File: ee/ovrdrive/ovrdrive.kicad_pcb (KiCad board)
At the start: 2 copper layers, 47.2 x 15.1 mm, 6 parts, among them J1 USB_A, U1 SM3257ENT, U2 JDEC_FLASH

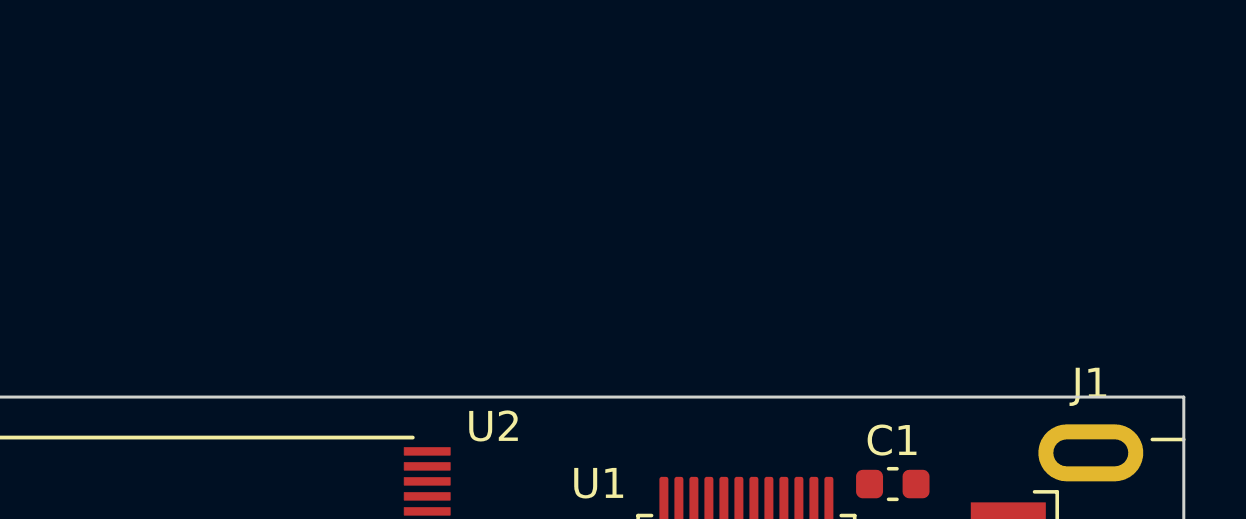
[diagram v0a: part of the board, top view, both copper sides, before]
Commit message: Updated the sm3257en to the correct pinout. Dropped some parts on the layout.
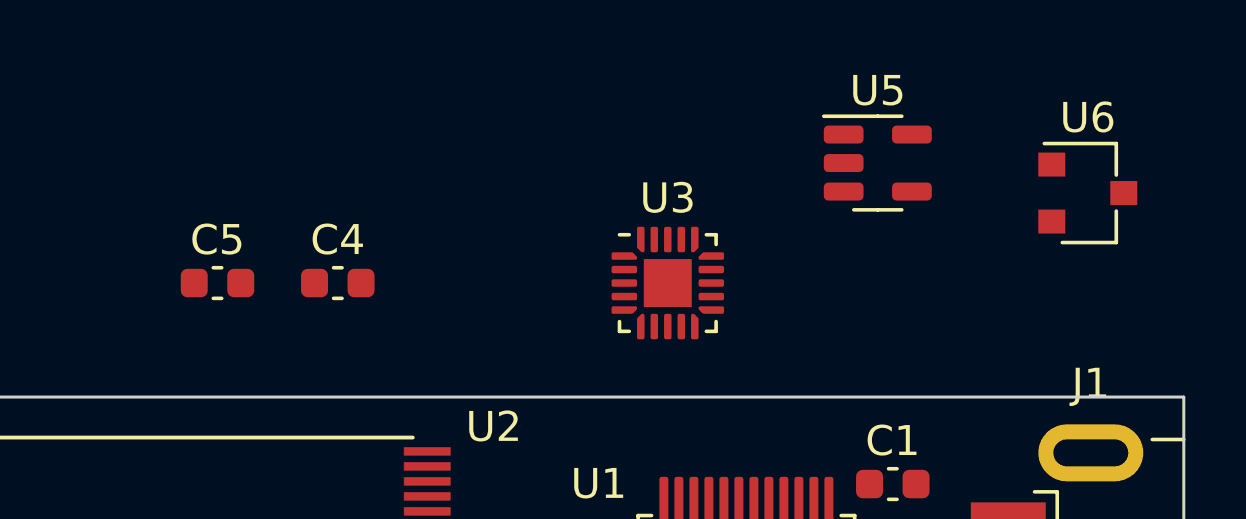
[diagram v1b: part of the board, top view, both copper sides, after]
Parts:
- added C4: 100nF, Capacitor_SMD:C_0603_1608Metric, F.Cu at (121.0, 75.0)
- added C5: 4.7uF, Capacitor_SMD:C_0603_1608Metric, F.Cu at (117.0, 75.0)
- added U3: ATtiny24A-MM, Package_DFN_QFN:QFN-20-1EP_3x3mm_P0.45mm_EP1.6x1.6mm, F.Cu at (132.0, 75.0)
- added U5: AD8001AR, Package_TO_SOT_SMD:SOT-23-5, F.Cu at (139.0, 71.0)
- added U6: TL431DCK, Package_TO_SOT_SMD:SC-59, F.Cu at (146.0, 72.0)
- U2: value JDEC_FLASH -> FLASH
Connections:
- C3 pad 1: unconnected-(C3-Pad1) -> +3.3V
- C3 pad 2: unconnected-(C3-Pad2) -> GND
- J1 pad 1: unconnected-(J1-Pad1) -> +5V
- J1 pad 4: unconnected-(J1-Pad4) -> GND
- J1 pad 5: unconnected-(J1-Pad5) -> GND
- U1 pad 22: unconnected-(U1-Pad22) -> GND
- U1 pad 36: unconnected-(U1-Pad36) -> GND
- U1 pad 37: unconnected-(U1-Pad37) -> +5V
- U1 pad 41: unconnected-(U1-Pad41) -> GND
- U1 pad 46: unconnected-(U1-Pad46) -> GND
- U1 pad 47: unconnected-(U1-Pad47) -> GND
- U1 pad 9: unconnected-(U1-Pad9) -> GND
- U2 pad 12: unconnected-(U2-Pad12) -> +3.3V
- U2 pad 13: unconnected-(U2-Pad13) -> GND
- U2 pad 36: unconnected-(U2-Pad36) -> GND
- U2 pad 37: unconnected-(U2-Pad37) -> +3.3V
- U2 pad 9: /~{CE} -> Net-(U2-Pad9)

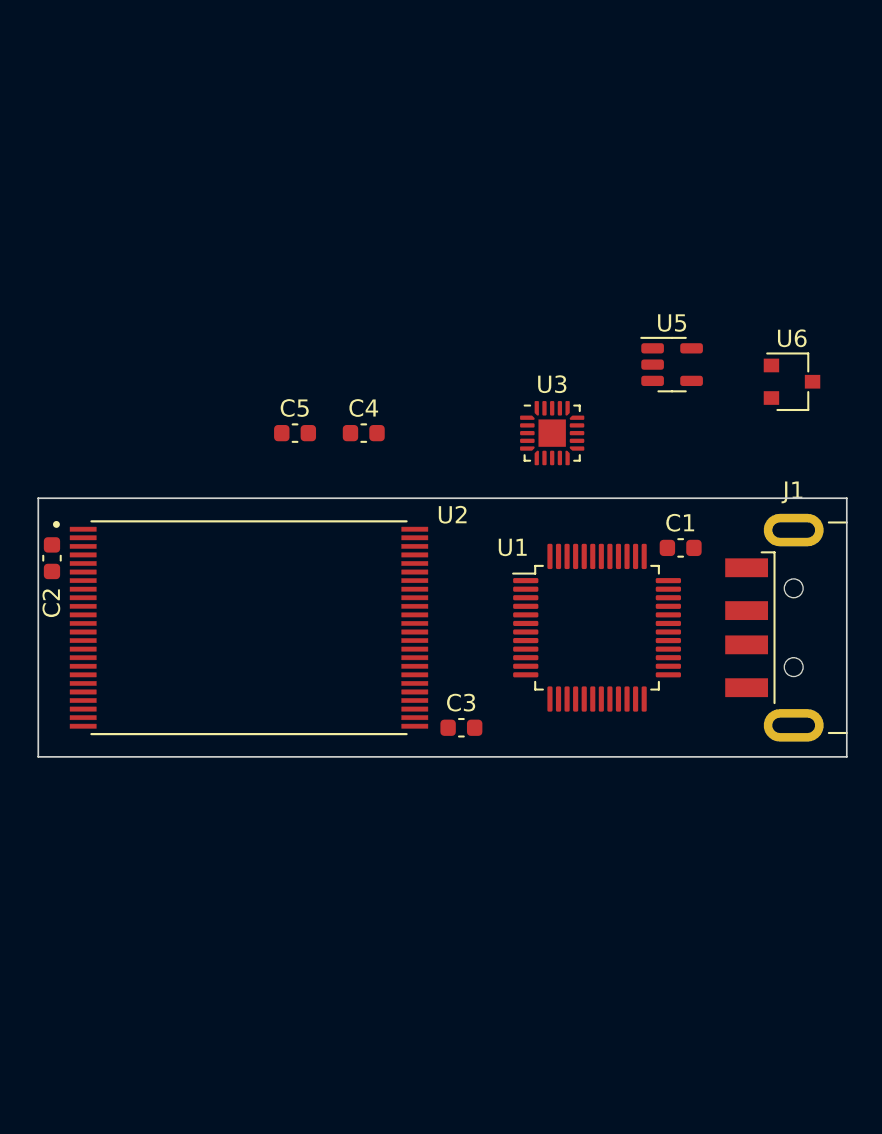
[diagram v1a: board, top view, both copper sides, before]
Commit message: Added a bunch of mech parts.
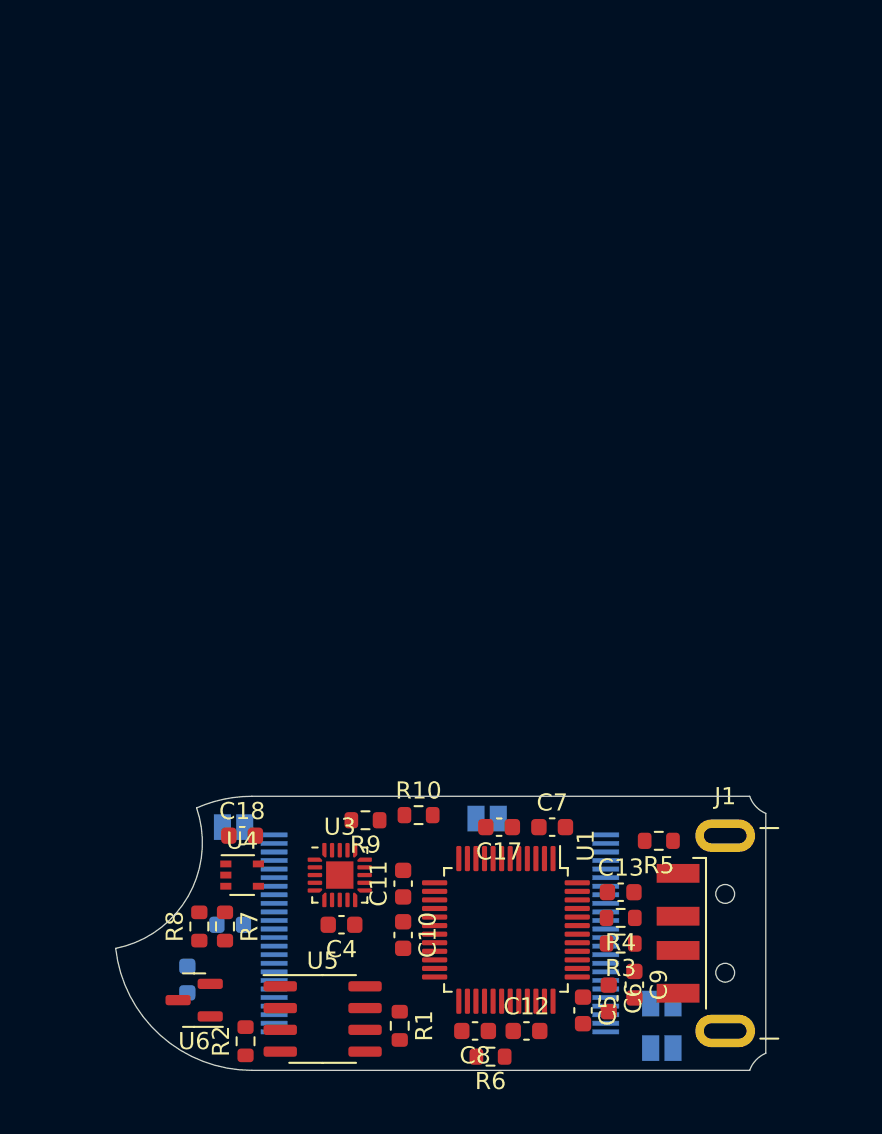
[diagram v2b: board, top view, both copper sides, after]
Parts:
- removed C3: 1uF, Capacitor_SMD:C_0603_1608Metric
- added C10: 1uF, Capacitor_SMD:C_0603_1608Metric, F.Cu at (123.3, 104.3)
- added C11: 1uF, Capacitor_SMD:C_0603_1608Metric, F.Cu at (123.3, 101.3)
- added C12: 1uF, Capacitor_SMD:C_0603_1608Metric, F.Cu at (130.5, 109.9)
- added C13: 1uF, Capacitor_SMD:C_0603_1608Metric, F.Cu at (136.0, 101.8)
- added C17: 1uF, Capacitor_SMD:C_0603_1608Metric, F.Cu at (128.9, 98.0)
- added C18: 100nF, Capacitor_SMD:C_0603_1608Metric, F.Cu at (113.9, 98.5)
- added C6: 4.7uF, Capacitor_SMD:C_0603_1608Metric, F.Cu at (135.3, 108.0)
- added C7: 4.7uF, Capacitor_SMD:C_0603_1608Metric, F.Cu at (132.0, 98.0)
- added C8: 1uF, Capacitor_SMD:C_0603_1608Metric, F.Cu at (127.5, 109.9)
- added C9: 1uF, Capacitor_SMD:C_0603_1608Metric, F.Cu at (136.8, 107.2)
- added JP1: SolderJumper_2_Open, Jumper:SolderJumper-2_P1.3mm_Open_Pad1.0x1.5mm, B.Cu at (138.4, 108.3)
- added JP2: SolderJumper_2_Open, Jumper:SolderJumper-2_P1.3mm_Open_Pad1.0x1.5mm, B.Cu at (138.4, 110.9)
- added JP3: SolderJumper_2_Open, Jumper:SolderJumper-2_P1.3mm_Open_Pad1.0x1.5mm, B.Cu at (113.4, 98.0)
- added JP4: SolderJumper_2_Open, Jumper:SolderJumper-2_P1.3mm_Open_Pad1.0x1.5mm, B.Cu at (128.2, 97.5)
- added R1: 10k, Resistor_SMD:R_0603_1608Metric, F.Cu at (123.1, 109.6)
- added R10: 680R, Resistor_SMD:R_0603_1608Metric, F.Cu at (124.2, 97.3)
- added R2: 747k, Resistor_SMD:R_0603_1608Metric, F.Cu at (114.1, 110.5)
- added R3: 2.2R, Resistor_SMD:R_0603_1608Metric, F.Cu at (136.0, 104.8)
- added R4: 2.2R, Resistor_SMD:R_0603_1608Metric, F.Cu at (136.0, 103.3)
- added R5: 2.2R, Resistor_SMD:R_0603_1608Metric, F.Cu at (138.2, 98.8)
- added R6: 1k, Resistor_SMD:R_0603_1608Metric, F.Cu at (128.4, 111.4)
- added R7: 10k, Resistor_SMD:R_0603_1608Metric, F.Cu at (112.9, 103.8)
- added R8: 10k, Resistor_SMD:R_0603_1608Metric, F.Cu at (111.4, 103.8)
- added R9: 1k, Resistor_SMD:R_0603_1608Metric, F.Cu at (121.1, 97.6)
- added U4: 74AUC1G32, Package_TO_SOT_SMD:SOT-353_SC-70-5, F.Cu at (113.9, 100.8)
- C1: value 1uF -> 100nF; moved to B.Cu
- C2, U2: moved to B.Cu
- C4: value 100nF -> 1uF
- U5: footprint Package_TO_SOT_SMD:SOT-23-5 -> Package_SO:SOIC-8_3.9x4.9mm_P1.27mm
- U6: value TL431DCK -> LM4040DBZ-2.5; footprint Package_TO_SOT_SMD:SC-59 -> Package_TO_SOT_SMD:SOT-23
- moved U6 50.2 mm to (111.1, 108.1), turned to 180 degrees
- moved U5 43.3 mm to (118.6, 109.2)
- moved C5 37.7 mm to (133.8, 108.7), turned to -90 degrees
- moved C1 34.3 mm to (113.2, 103.7), turned to 180 degrees
- moved C4 28.7 mm to (119.7, 103.7), turned to 180 degrees
- moved U3 28.6 mm to (119.6, 100.8)
- moved C2 25.8 mm to (110.7, 106.9)
- moved U2 21.0 mm to (125.4, 104.2), turned to 180 degrees
- moved U1 18.4 mm to (129.3, 104.0), turned to -90 degrees
- moved J1 18.3 mm to (149.0, 104.2)
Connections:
- C1 pad 1: unconnected-(C1-Pad1) -> +3.3V
- C1 pad 2: unconnected-(C1-Pad2) -> GND
- C2 pad 1: unconnected-(C2-Pad1) -> +3.3V
- C2 pad 2: unconnected-(C2-Pad2) -> GND
- C4 pad 1: +3.3V -> +5V
- J1 pad 1: +5V -> Net-(J1-Pad1)
- J1 pad 2: unconnected-(J1-Pad2) -> Net-(J1-Pad2)
- J1 pad 3: unconnected-(J1-Pad3) -> Net-(J1-Pad3)
- U1 pad 14: unconnected-(U1-Pad14) -> +3.3V
- U1 pad 15: unconnected-(U1-Pad15) -> +3.3V
- U1 pad 16: unconnected-(U1-Pad16) -> +1V8
- U1 pad 17: unconnected-(U1-Pad17) -> +3.3V
- U1 pad 2: unconnected-(U1-Pad2) -> /RB1
- U1 pad 27: unconnected-(U1-Pad27) -> Net-(R6-Pad2)
- U1 pad 28: unconnected-(U1-Pad28) -> +3.3V
- U1 pad 29: unconnected-(U1-Pad29) -> +1V8
- U1 pad 3: unconnected-(U1-Pad3) -> +1V8
- U1 pad 30: unconnected-(U1-Pad30) -> +3.3V
- U1 pad 31: unconnected-(U1-Pad31) -> /DQS
- U1 pad 32: unconnected-(U1-Pad32) -> Net-(JP1-Pad2)
- U1 pad 33: unconnected-(U1-Pad33) -> Net-(JP2-Pad2)
- U1 pad 34: unconnected-(U1-Pad34) -> /~{CE3}
- U1 pad 35: unconnected-(U1-Pad35) -> /~{CE2}
- U1 pad 38: unconnected-(U1-Pad38) -> +3.3V
- U1 pad 39: unconnected-(U1-Pad39) -> +3.3V
- U1 pad 4: unconnected-(U1-Pad4) -> +3.3V
- U1 pad 40: unconnected-(U1-Pad40) -> +1V8
- U1 pad 42: unconnected-(U1-Pad42) -> /DM
- U1 pad 43: unconnected-(U1-Pad43) -> /DP
- U1 pad 44: unconnected-(U1-Pad44) -> Net-(JP4-Pad2)
- U1 pad 45: unconnected-(U1-Pad45) -> +3.3V
- U1 pad 5: unconnected-(U1-Pad5) -> /RB0
- U1 pad 8: unconnected-(U1-Pad8) -> /~{CE1}
- U3 pad 1: unconnected-(U3-Pad1) -> /SCK
- U3 pad 13: unconnected-(U3-Pad13) -> /~{RST}
- U3 pad 15: unconnected-(U3-Pad15) -> Net-(D1-Pad2)
- U3 pad 16: unconnected-(U3-Pad16) -> /MOSI
- U3 pad 20: unconnected-(U3-Pad20) -> /MISO
- U3 pad 21: Net-(U3-Pad21) -> GND
- U3 pad 3: unconnected-(U3-Pad3) -> Net-(R7-Pad2)
- U3 pad 4: unconnected-(U3-Pad4) -> /Vs
- U3 pad 8: Net-(U3-Pad21) -> GND
- U3 pad 9: unconnected-(U3-Pad9) -> +5V
- U5 pad 2: unconnected-(U5-Pad2) -> /Vs
- U5 pad 3: unconnected-(U5-Pad3) -> Net-(J2-Pad2)
- U5 pad 4: unconnected-(U5-Pad4) -> GND
- U6 pad 1: unconnected-(U6-Pad1) -> Net-(R1-Pad2)
- U6 pad 2: (no net) -> /Vs
- U6 pad 3: unconnected-(U6-Pad3) -> (no net)
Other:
- board size 47.2 x 15.1 mm -> 38 x 16 mm

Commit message: Mech looking decent, new USB to fit in case.
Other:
- copper layers 2 -> 4
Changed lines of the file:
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@@
 (kicad_pcb (version 20211014) (generator pcbnew)
   (general
-    (thickness 1.6)
+    (thickness 0.799)
   )
   (paper "A4")
   (layers
     (0 "F.Cu" signal)
+    (1 "In1.Cu" signal)
+    (2 "In2.Cu" signal)
     (31 "B.Cu" signal)
     (32 "B.Adhes" user "B.Adhesive")
@@
   )
   (setup
+    (stackup
+      (layer "F.SilkS" (type "Top Silk Screen"))
+      (layer "F.Paste" (type "Top Solder Paste"))
+      (layer "F.Mask" (type "Top Solder Mask") (thickness 0.01))
+      (layer "F.Cu" (type "copper") (thickness 0.035))
+      (layer "dielectric 1" (type "core") (thickness 0.213) (material "FR4") (epsilon_r 4.5) (loss_tangent 0.02))
+      (layer "In1.Cu" (type "copper") (thickness 0.035))
+      (layer "dielectric 2" (type "prepreg") (thickness 0.213) (material "FR4") (epsilon_r 4.5) (loss_tangent 0.02))
+      (layer "In2.Cu" (type "copper") (thickness 0.035))
+      (layer "dielectric 3" (type "core") (thickness 0.213) (material "FR4") (epsilon_r 4.5) (loss_tangent 0.02))
+      (layer "B.Cu" (type "copper") (thickness 0.035))
+      (layer "B.Mask" (type "Bottom Solder Mask") (thickness 0.01))
+      (layer "B.Paste" (type "Bottom Solder Paste"))
+      (layer "B.SilkS" (type "Bottom Silk Screen"))
+      (copper_finish "None")
+      (dielectric_constraints no)
+    )
     (pad_to_mask_clearance 0)
     (pcbplotparams
@@
     )
   )
-  (footprint "Connector_USB:USB_A_CNCTech_1001-011-01101_Horizontal" (layer "F.Cu")
+  (footprint "Connector_USB:USB_A_CNCTech_1001-011-01101_Horizontal" locked (layer "F.Cu")
     (at 149 104.2)
     (descr "USB type A Plug, Horizontal, http://cnctech.us/pdfs/1001-011-01101.pdf")
@@
     (fp_circle (center -6.9 -2.3) (end -6.9 -2.8) (layer "F.Fab") (width 0.1) (fill none))
     (fp_circle (center -6.9 2.3) (end -6.9 2.8) (layer "F.Fab") (width 0.1) (fill none))
-    (pad "" np_thru_hole circle (at -6.9 2.3) (size 1.1 1.1) (drill 1.1) (layers *.Cu *.Mask))
-    (pad "" np_thru_hole circle (at -6.9 -2.3) (size 1.1 1.1) (drill 1.1) (layers *.Cu *.Mask))
-    (pad "1" smd rect (at -9.65 -3.5) (size 2.5 1.1) (layers "F.Cu" "F.Paste" "F.Mask")
+    (pad "" np_thru_hole circle locked (at -6.9 2.3) (size 1.1 1.1) (drill 1.1) (layers *.Cu *.Mask))
+    (pad "" np_thru_hole circle locked (at -6.9 -2.3) (size 1.1 1.1) (drill 1.1) (layers *.Cu *.Mask))
+    (pad "1" smd rect locked (at -9.65 -3.5) (size 2.5 1.1) (layers "F.Cu" "F.Paste" "F.Mask")
       (net 5 "Net-(J1-Pad1)") (pinfunction "VBUS") (pintype "power_in"))
-    (pad "2" smd rect (at -9.65 -1) (size 2.5 1.1) (layers "F.Cu" "F.Paste" "F.Mask")
+    (pad "2" smd rect locked (at -9.65 -1) (size 2.5 1.1) (layers "F.Cu" "F.Paste" "F.Mask")
       (net 4 "Net-(J1-Pad2)") (pinfunction "D-") (pintype "bidirectional"))
-    (pad "3" smd rect (at -9.65 1) (size 2.5 1.1) (layers "F.Cu" "F.Paste" "F.Mask")
+    (pad "3" smd rect locked (at -9.65 1) (size 2.5 1.1) (layers "F.Cu" "F.Paste" "F.Mask")
       (net 3 "Net-(J1-Pad3)") (pinfunction "D+") (pintype "bidirectional"))
-    (pad "4" smd rect (at -9.65 3.5) (size 2.5 1.1) (layers "F.Cu" "F.Paste" "F.Mask")
+    (pad "4" smd rect locked (at -9.65 3.5) (size 2.5 1.1) (layers "F.Cu" "F.Paste" "F.Mask")
       (net 79 "GND") (pinfunction "GND") (pintype "power_in"))
-    (pad "5" thru_hole oval (at -6.9 -5.7) (size 3.5 1.9) (drill oval 2.5 0.9) (layers *.Cu *.Mask)
+    (pad "5" thru_hole oval locked (at -6.9 -5.7) (size 3.5 1.9) (drill oval 2.5 0.9) (layers *.Cu *.Mask)
       (net 79 "GND") (pinfunction "Shield") (pintype "passive"))
-    (pad "5" thru_hole oval (at -6.9 5.7) (size 3.5 1.9) (drill oval 2.5 0.9) (layers *.Cu *.Mask)
+    (pad "5" thru_hole oval locked (at -6.9 5.7) (size 3.5 1.9) (drill oval 2.5 0.9) (layers *.Cu *.Mask)
       (net 79 "GND") (pinfunction "Shield") (pintype "passive"))
-    (model "${KIPRJMOD}/../lib/3d/1001-011-01101.step"
-      (offset (xyz 11 0 1))
-      (scale (xyz 1 1 1))
-      (rotate (xyz -180 0 90))
-    )
-  )
+    (model "${KIPRJMOD}/../lib/3d/480372200.step"
+      (offset (xyz 1.5 0 0))
+      (scale (xyz 1 1 1))
+      (rotate (xyz 90 180 90))
+    )
+  )

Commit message: Fit seems to be working.
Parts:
- removed JP3, JP4: SolderJumper_2_Open, Jumper:SolderJumper-2_P1.3mm_Open_Pad1.0x1.5mm
- added C14: 100nF, Capacitor_SMD:C_0603_1608Metric, B.Cu at (142.4, 104.2)
- added C3: 100nF, Capacitor_SMD:C_0603_1608Metric, B.Cu at (137.0, 103.8)
- added D1: LED, LED_SMD:LED_0603_1608Metric, B.Cu at (111.8, 105.4)
- added D2: D, Diode_SMD:D_0603_1608Metric, B.Cu at (139.6, 100.4)
- added D3: D, Diode_SMD:D_0603_1608Metric, B.Cu at (139.6, 101.9)
- added Q1: Q_NMOS_DGS, Package_TO_SOT_SMD:SOT-23, B.Cu at (139.7, 104.5)
- added R11: 2.2R, Resistor_SMD:R_0603_1608Metric, B.Cu at (141.8, 107.9)
- R10: moved to B.Cu
- U5: value AD8001AR -> LMV321; footprint Package_SO:SOIC-8_3.9x4.9mm_P1.27mm -> Package_TO_SOT_SMD:SOT-23-5
- moved R10 13.5 mm to (137.7, 97.4), turned to 180 degrees
- moved R1 4.41 mm to (118.8, 110.6), turned to 180 degrees
- moved C2 4.06 mm to (113.2, 103.7), turned to 180 degrees
- moved R2 3.76 mm to (117.0, 108.1)
- moved U6 3.10 mm to (114.2, 108.0)
- moved U5 1.70 mm to (119.9, 108.1)
- moved C1 1.50 mm to (113.2, 102.2)
- moved C12 0.60 mm to (130.5, 109.3)
- moved C5 0.60 mm to (133.8, 108.1)
- moved C8 0.60 mm to (127.5, 109.3)
- moved C9 0.60 mm to (136.8, 106.6)
- moved R6 0.60 mm to (128.4, 110.8)
- moved C13 0.60 mm to (136.0, 101.2)
- moved C17 0.60 mm to (128.9, 97.4)
- moved C6 0.60 mm to (135.3, 107.4)
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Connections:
- R10 pad 2: Net-(JP4-Pad1) -> Net-(U1-Pad44)
- U1 pad 44: Net-(JP4-Pad2) -> Net-(U1-Pad44)
- U3 pad 2: unconnected-(U3-Pad2) -> /KILL
- U3 pad 5: unconnected-(U3-Pad5) -> /Distruct_PWM
- U4 pad 4: Net-(JP3-Pad2) -> Net-(U2-Pad9)
- U5 pad 1: unconnected-(U5-Pad1) -> Net-(J2-Pad2)
- U5 pad 2: /Vs -> GND
- U5 pad 3: Net-(J2-Pad2) -> /Vs
- U5 pad 4: GND -> /Vs
- U5 pad 5: unconnected-(U5-Pad5) -> +5V
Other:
- board size 38 x 16 mm -> 37.2 x 15 mm
